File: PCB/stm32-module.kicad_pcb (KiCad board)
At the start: 4 copper layers, 45.5 x 78.5 mm, 35 parts, among them J1 Conn_01x30_Socket, J2 Conn_01x30_Socket, J3 TYPE-C_16PIN_2MD__073_

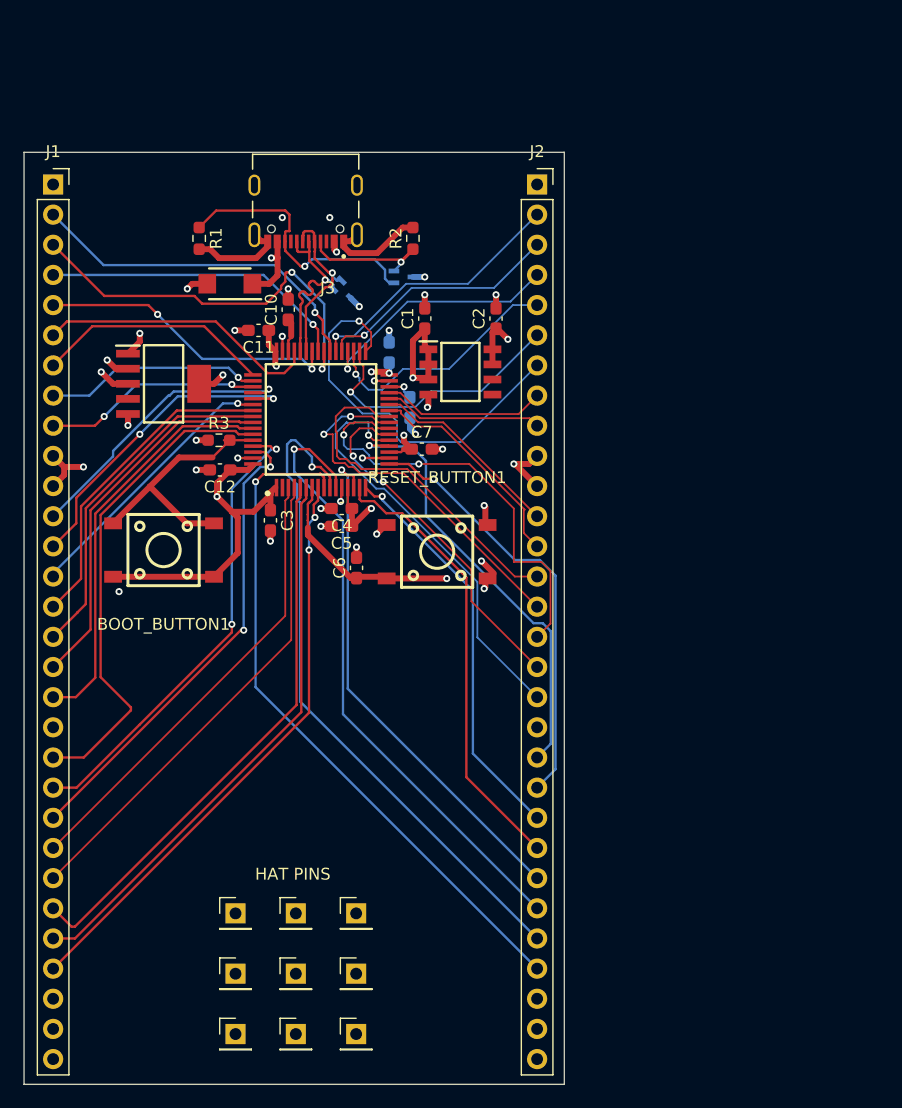
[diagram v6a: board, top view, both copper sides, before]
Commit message: Delay tuned USB traces
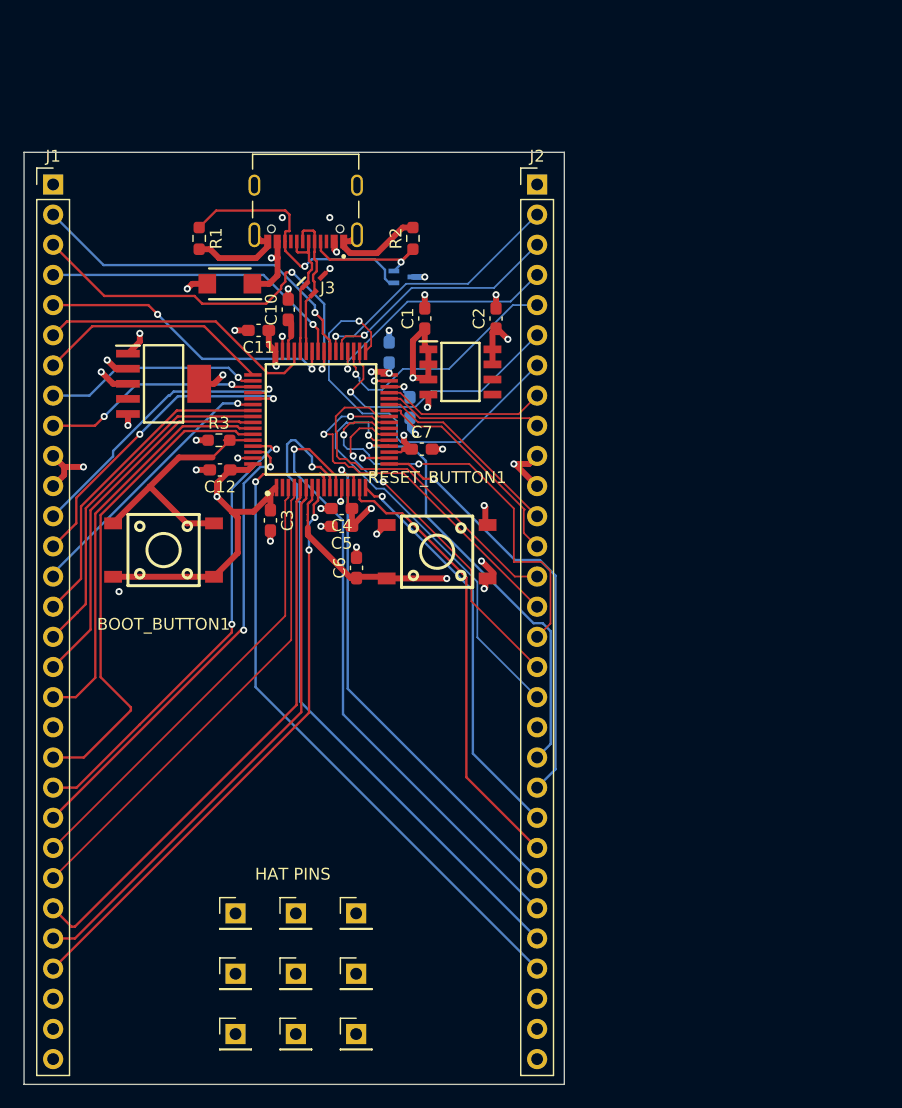
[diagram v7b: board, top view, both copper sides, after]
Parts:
- DATAESD1: moved to F.Cu
- J1, J2: footprint REQUIRED:PinSocket_1x30_P2.54mm_Vertical -> Connector_PinHeader_2.54mm:PinHeader_1x30_P2.54mm_Vertical
- moved DATAESD1 2.49 mm to (105.8, 48.5), turned to 45 degrees
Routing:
- net /D+: track 15.9 -> 12.6 mm, vias 1 -> 0
- net /D-: track 14.8 -> 12.5 mm, vias 1 -> 0

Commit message: Changed ldo due to availability
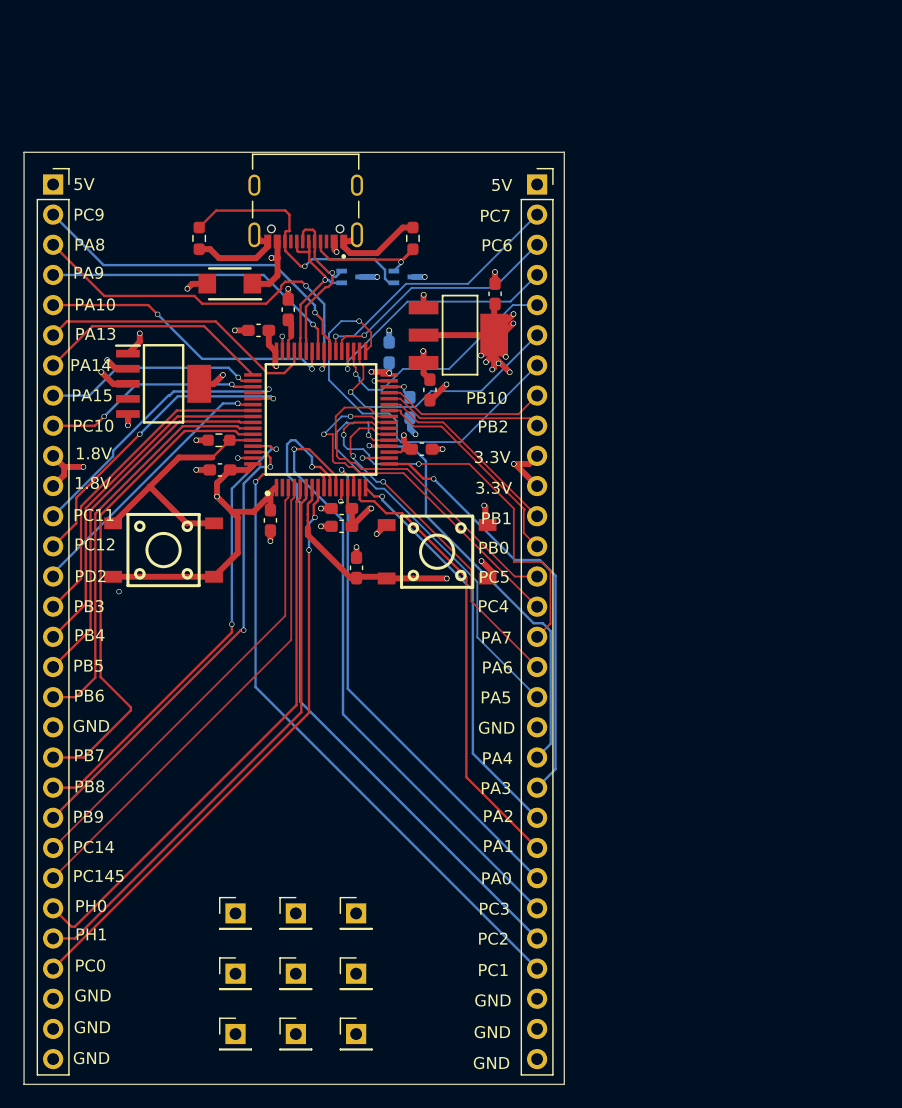
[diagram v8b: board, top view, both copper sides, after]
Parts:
- removed C1: 4.7uF 16V, REQUIRED:C_0603_1608Metric_Pad1.08x0.95mm_HandSolder
- removed C2: 1uF 10V, REQUIRED:C_0603_1608Metric_Pad1.08x0.95mm_HandSolder
- added C13: 1uF 10V, Capacitor_SMD:C_0603_1608Metric_Pad1.08x0.95mm_HandSolder, F.Cu at (120.9, 49.4)
- added C14: 1uF 10V, Capacitor_SMD:C_0603_1608Metric_Pad1.08x0.95mm_HandSolder, F.Cu at (115.4, 57.5)
- 3.3VLDO1: value MCP1726-3302E_SNVAO -> BL8072CLTR33; footprint REQUIRED:SOIC127P600X175-8N -> easyeda2kicad:SOT-223-3_L6.5-W3.4-P2.30-LS7.0-BR
- BOOT_BUTTON1, RESET_BUTTON1: footprint REQUIRED:SW-SMD_4P-L6.2-W6.0-P4.50-LS9.0 -> easyeda2kicad:SW-SMD_4P-L6.2-W6.0-P4.50-LS9.0
- C10, C11, C12, C3, C4, C5, C6, C7, C8, C9: footprint REQUIRED:C_0603_1608Metric_Pad1.08x0.95mm_HandSolder -> Capacitor_SMD:C_0603_1608Metric_Pad1.08x0.95mm_HandSolder
- DATAESD1: moved to B.Cu
- J1, J2: footprint Connector_PinHeader_2.54mm:PinHeader_1x30_P2.54mm_Vertical -> Connector_PinSocket_2.54mm:PinSocket_1x30_P2.54mm_Vertical
- J3: footprint REQUIRED:SHOUHAN_TYPE-C_16PIN_2MD__073_ -> TYPE-C_16PIN_2MD__073_:SHOUHAN_TYPE-C_16PIN_2MD__073_
- R1, R2, R3: footprint REQUIRED:R_0603_1608Metric_Pad0.98x0.95mm_HandSolder -> Resistor_SMD:R_0603_1608Metric_Pad0.98x0.95mm_HandSolder
- moved 3.3VLDO1 3.10 mm to (117.9, 52.9), turned to 180 degrees
- moved DATAESD1 3.00 mm to (108.8, 48.0), turned to 0 degrees
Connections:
- 3.3VLDO1 pad 1: /VBUS -> GND
- 3.3VLDO1 pad 2: /VBUS -> +3.3V
- 3.3VLDO1 pad 4: GND -> +3.3V
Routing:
- net +3.3V: track 141.3 -> 166.8 mm, vias 10 -> 17
- net /VBUS: track 91.8 -> 86.2 mm, vias 5 -> 3
- net /D-: track 12.5 -> 15.2 mm, vias 0 -> 1
- net /D+: track 12.6 -> 14.1 mm, vias 0 -> 1
- net /PA8: track 34.7 -> 33.7 mm
- net GND: track 157.1 -> 157.3 mm, vias 28 -> 27
- added copper zone on In1.Cu, net +3.3V
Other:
- board text added: "1.8V"
- board text added: "3.3V"
- board text added: "5V"
- board text added: "GND"
- board text added: "PA0"
- board text added: "PA1"
- board text added: "PA10"
- board text added: "PA13"
- board text added: "PA14"
- board text added: "PA15"
- board text added: "PA2"
- board text added: "PA3"
- board text added: "PA4"
- board text added: "PA5"
- board text added: "PA6"
- board text added: "PA7"
- board text added: "PA8"
- board text added: "PA9"
- board text added: "PB0"
- board text added: "PB1"
- board text added: "PB10"
- board text added: "PB12"
- board text added: "PB13"
- board text added: "PB14"
- board text added: "PB15"
- board text added: "PB2"
- board text added: "PB3"
- board text added: "PB4"
- board text added: "PB5"
- board text added: "PB6"
- board text added: "PB7"
- board text added: "PB8"
- board text added: "PB9"
- board text added: "PC0"
- board text added: "PC1"
- board text added: "PC10"
- board text added: "PC11"
- board text added: "PC12"
- board text added: "PC14"
- board text added: "PC145"
- board text added: "PC2"
- board text added: "PC3"
- board text added: "PC4"
- board text added: "PC5"
- board text added: "PC6"
- board text added: "PC7"
- board text added: "PC9"
- board text added: "PD2"
- board text added: "PH0"
- board text added: "PH1"
- board text removed: "HAT PINS"
